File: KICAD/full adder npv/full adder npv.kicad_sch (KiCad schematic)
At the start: 24 parts, among them J2 Barrel_Jack, SW1 SW_SPDT, SW10 SW_SPDT, SW11 SW_SPDT, SW12 SW_SPDT, SW13 SW_SPDT, SW14 SW_SPDT, SW15 SW_SPDT, SW16 SW_SPDT, SW2 SW_SPDT, SW3 SW_SPDT, SW4 SW_SPDT, SW5 SW_SPDT, SW6 SW_SPDT, SW7 SW_SPDT, SW8 SW_SPDT, SW9 SW_SPDT

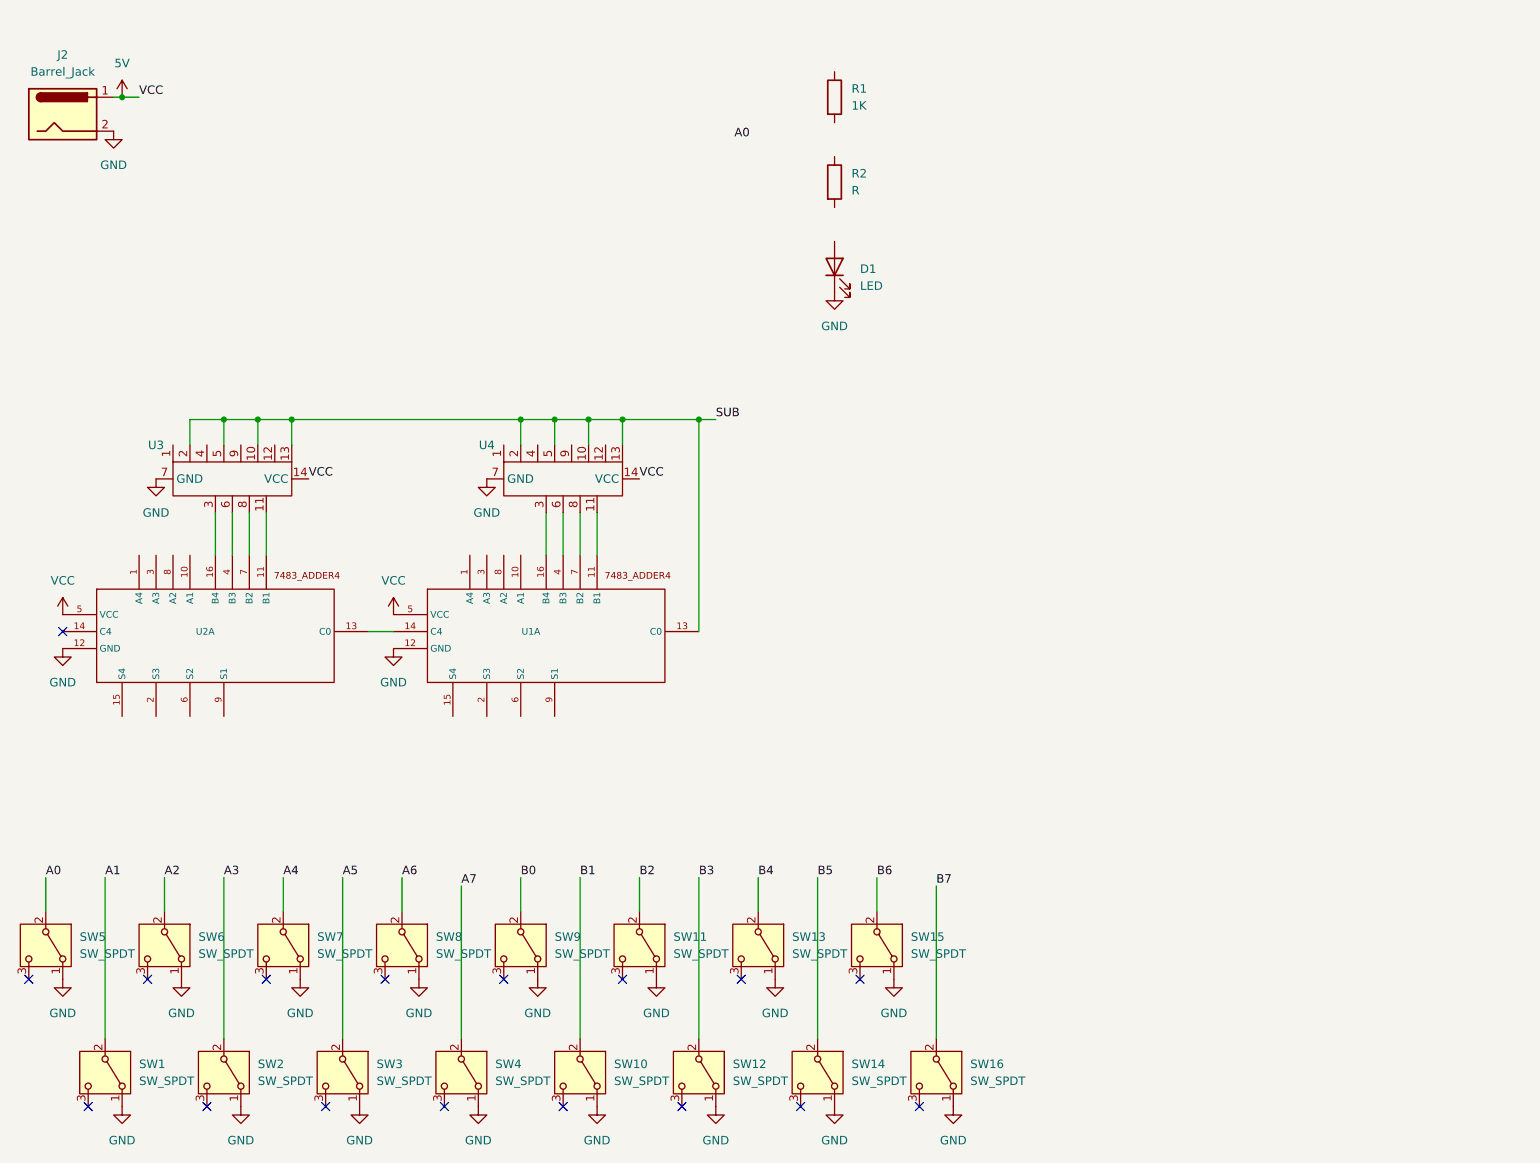
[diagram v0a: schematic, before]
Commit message: Update full adder npv.kicad_sch
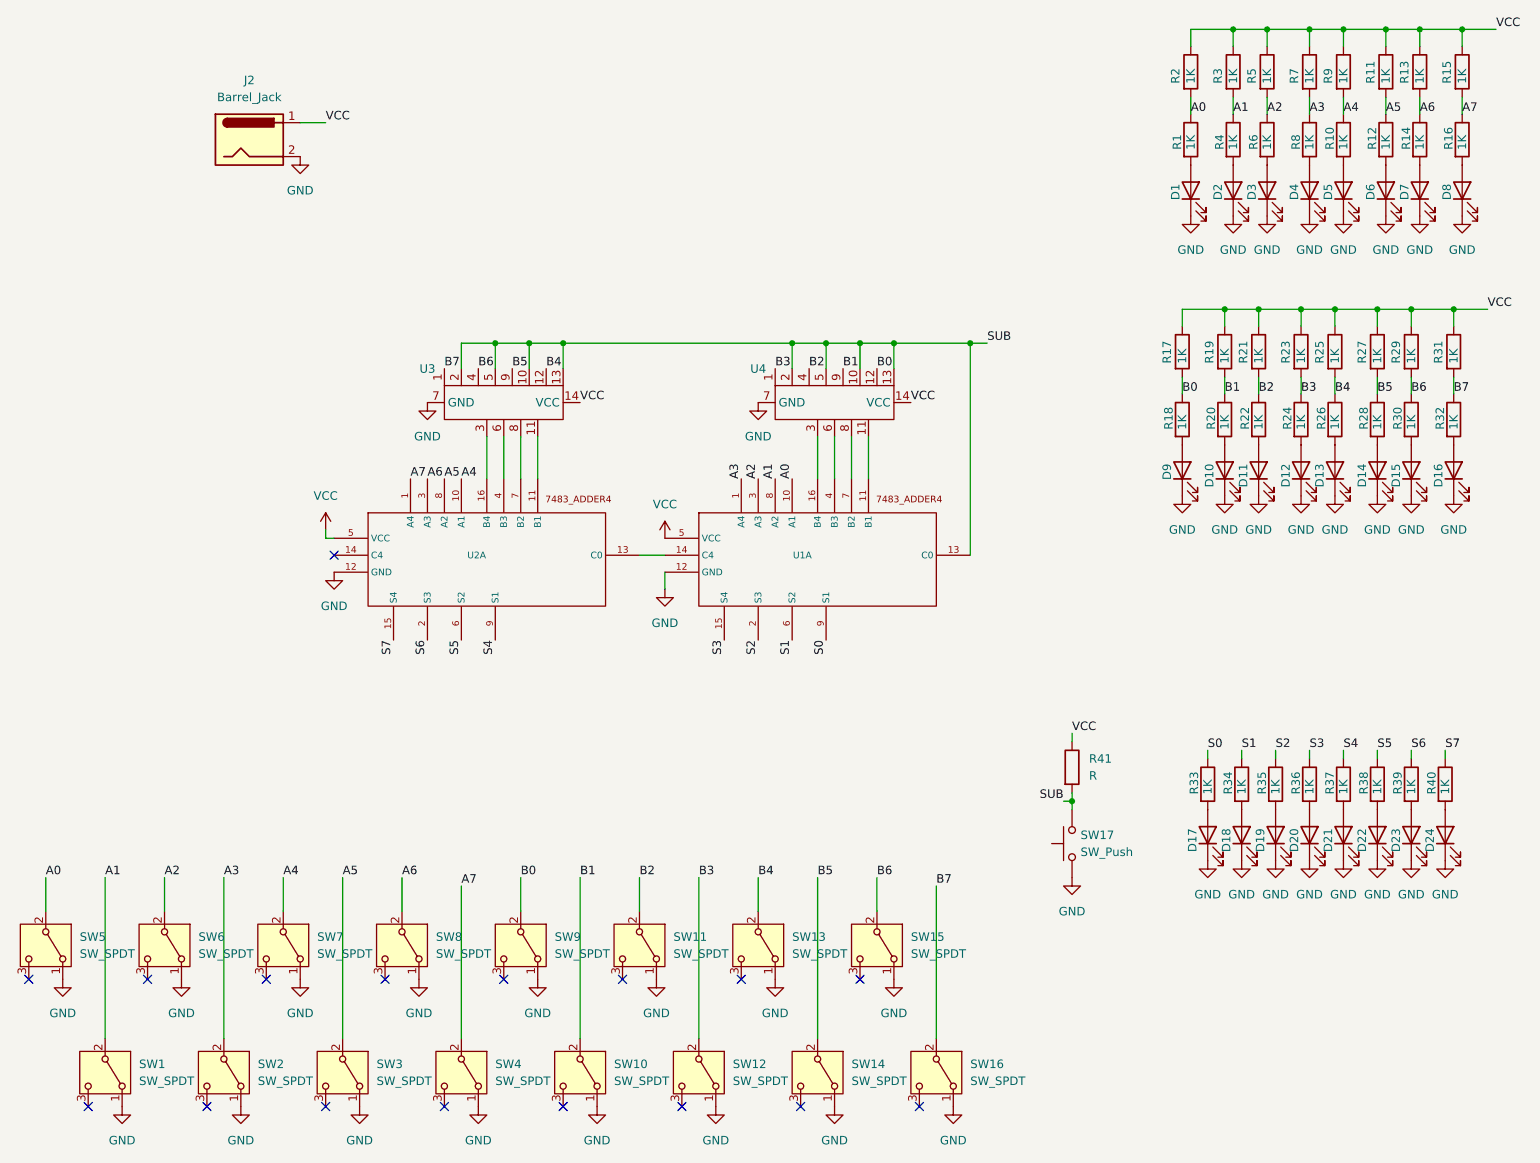
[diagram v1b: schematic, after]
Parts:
- added D10, D11, D12, D13, D14, D15, D16, D17, D18, D19, D2, D20, D21, D22, D23, D24, D3, D4, D5, D6, D7, D8, D9: LED, symbol Device:LED
- added R10, R11, R12, R13, R14, R15, R16, R17, R18, R19, R20, R21, R22, R23, R24, R25, R26, R27, R28, R29, R3, R30, R31, R32, R33, R34, R35, R36, R37, R38, R39, R4, R40, R5, R6, R7, R8, R9: 1K, symbol Device:R
- added R41: R, symbol Device:R
- added SW17: SW_Push, symbol Switch:SW_Push
- R2: value R -> 1K
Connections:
- net 5V is gone; now on net VCC: J2.1, U1.5 (VCC), U2.5 (VCC), U3.14 (VCC), U4.14 (VCC)
- net A0: now also R1.1, R2.2, U1.10 (A1)
- net A1: now also U1.8 (A2), R3.2, R4.1
- net A2: now also U1.3 (A3), R5.2, R6.1
- net A3: now also U1.1 (A4), R7.2, R8.1
- net A4: now also U2.10 (A1), R10.1, R9.2
- net A5: now also U2.8 (A2), R11.2, R12.1
- net A6: now also U2.3 (A3), R13.2, R14.1
- net A7: now also U2.1 (A4), R15.2, R16.1
- net B0: now also U4.12, R17.2, R18.1
- net B1: now also U4.9, R19.2, R20.1
- net B2: now also U4.4, R21.2, R22.1
- net B3: now also U4.1, R23.2, R24.1
- net B4: now also U3.12, R25.2, R26.1
- net B5: now also U3.9, R27.2, R28.1
- net B6: now also U3.4, R29.2, R30.1
- net B7: now also U3.1, R31.2, R32.1
- net GND: now also D10.1 (K), D11.1 (K), D12.1 (K), D13.1 (K), D14.1 (K), D15.1 (K), D16.1 (K), D17.1 (K), D18.1 (K), D19.1 (K), D2.1 (K), D20.1 (K), D21.1 (K), D22.1 (K), D23.1 (K), D24.1 (K), D3.1 (K), D4.1 (K), D5.1 (K), D6.1 (K), D7.1 (K), D8.1 (K), D9.1 (K), SW17.1
- net SUB: now also R41.2, SW17.2
- net VCC: now reaches R2.1
- net VCC: now also R11.1, R13.1, R15.1, R17.1, R19.1, R21.1, R23.1, R25.1, R27.1, R29.1, R3.1, R31.1, R41.1, R5.1, R7.1, R9.1
- net at D1.2 (A): now also R1.2
- net S7: now reaches U2.15 (S4)
- net S7: now also R40.1
- net S6: now reaches U2.2 (S3)
- net S6: now also R39.1
- net S5: now reaches U2.6 (S2)
- net S5: now also R38.1
- net S4: now reaches U2.9 (S1)
- net S4: now also R37.1
- net S3: now reaches U1.15 (S4)
- net S3: now also R36.1
- net S2: now reaches U1.2 (S3)
- net S2: now also R35.1
- net S1: now reaches U1.6 (S2)
- net S1: now also R34.1
- net S0: now reaches U1.9 (S1)
- net S0: now also R33.1
- new net: D7.2 (A), R14.2
- new net: D8.2 (A), R16.2
- new net: D16.2 (A), R32.2
- new net: D21.2 (A), R37.2
- new net: D17.2 (A), R33.2
- new net: D9.2 (A), R18.2
- new net: D19.2 (A), R35.2
- new net: D10.2 (A), R20.2
- new net: D13.2 (A), R26.2
- new net: D20.2 (A), R36.2
- new net: D18.2 (A), R34.2
- new net: D14.2 (A), R28.2
- new net: D6.2 (A), R12.2
- new net: D22.2 (A), R38.2
- new net: D15.2 (A), R30.2
- new net: D4.2 (A), R8.2
- new net: D5.2 (A), R10.2
- new net: D23.2 (A), R39.2
- new net: D11.2 (A), R22.2
- new net: D3.2 (A), R6.2
- new net: D24.2 (A), R40.2
- new net: D12.2 (A), R24.2
- new net: D2.2 (A), R4.2
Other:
- moved on the sheet: D1, J2, R1, U1A, U2A, U3, U4

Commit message: abc
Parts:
- D1, D10, D11, D12, D13, D14, D15, D16, D17, D18, D19, D2, D20, D21, D22, D23, D24, D3, D4, D5, D6, D7, D8, D9: footprint (none) -> LED_THT:LED_D3.0mm
- R1, R10, R11, R12, R13, R14, R15, R16, R17, R18, R19, R2, R20, R21, R22, R23, R24, R25, R26, R27, R28, R29, R3, R30, R31, R32, R33, R34, R35, R36, R37, R38, R39, R4, R40, R41, R5, R6, R7, R8, R9: footprint (none) -> Resistor_THT:R_Axial_DIN0204_L3.6mm_D1.6mm_P5.08mm_Horizontal
- U1, U2, U3, U4: footprint (none) -> Package_DIP:DIP-16_W7.62mm

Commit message: abc
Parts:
- J2: footprint (none) -> Connector_BarrelJack:BarrelJack_Horizontal
- SW1, SW10, SW11, SW12, SW13, SW14, SW15, SW16, SW17, SW2, SW3, SW4, SW5, SW6, SW7, SW8, SW9: footprint (none) -> Library:switch1
- U3, U4: footprint Package_DIP:DIP-16_W7.62mm -> Package_DIP:DIP-14_W7.62mm
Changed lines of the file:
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@@
 			)
 		)
-		(property "Footprint" "Package_DIP:DIP-16_W7.62mm"
+		(property "Footprint" "Package_DIP:DIP-14_W7.62mm"
 			(at 97.79 78.74 0)
 			(effects
@@
 			)
 		)
-		(property "Footprint" ""
+		(property "Footprint" "Library:switch1"
 			(at 54.61 179.07 0)
 			(effects
@@
 			)
 		)
-		(property "Footprint" ""
+		(property "Footprint" "Library:switch1"
 			(at 125.73 179.07 0)
 			(effects
@@
 			)
 		)
-		(property "Footprint" ""
+		(property "Footprint" "Library:switch1"
 			(at 63.5 160.02 0)
 			(effects
@@
 			)
 		)
-		(property "Footprint" ""
+		(property "Footprint" "Library:switch1"
 			(at 36.83 179.07 0)
 			(effects
@@
 			)
 		)
-		(property "Footprint" "Package_DIP:DIP-16_W7.62mm"
+		(property "Footprint" "Package_DIP:DIP-14_W7.62mm"
 			(at 147.32 78.74 0)
 			(effects
@@
 			)
 		)
-		(property "Footprint" ""
+		(property "Footprint" "Library:switch1"
 			(at 45.72 160.02 0)
 			(effects
@@
 			)
 		)
-		(property "Footprint" ""
+		(property "Footprint" "Library:switch1"
 			(at 72.39 179.07 0)
 			(effects
@@
 			)
 		)
-		(property "Footprint" ""
+		(property "Footprint" "Library:switch1"
 			(at 116.84 160.02 0)
 			(effects
@@
 			)
 		)
-		(property "Footprint" ""
+		(property "Footprint" "Library:switch1"
 			(at 90.17 179.07 0)
 			(effects
@@
 			)
 		)
-		(property "Footprint" ""
+		(property "Footprint" "Library:switch1"
 			(at 152.4 160.02 0)
 			(effects
@@
 			)
 		)
-		(property "Footprint" ""
+		(property "Footprint" "Library:switch1"
 			(at 81.28 160.02 0)
 			(effects
@@
 			)
 		)
-		(property "Footprint" ""
+		(property "Footprint" "Connector_BarrelJack:BarrelJack_Horizontal"
 			(at 59.69 40.386 0)
 			(effects
@@
 			)
 		)
-		(property "Footprint" ""
+		(property "Footprint" "Library:switch1"
 			(at 107.95 179.07 0)
 			(effects
@@
 			)
 		)
-		(property "Footprint" ""
+		(property "Footprint" "Library:switch1"
 			(at 176.53 144.78 0)
 			(effects
@@
 			)
 		)
-		(property "Footprint" ""
+		(property "Footprint" "Library:switch1"
 			(at 27.94 160.02 0)
 			(effects
@@
 			)
 		)
-		(property "Footprint" ""
+		(property "Footprint" "Library:switch1"
 			(at 99.06 160.02 0)
 			(effects
@@
 			)
 		)
-		(property "Footprint" ""
+		(property "Footprint" "Library:switch1"
 			(at 161.29 179.07 0)
 			(effects
@@
 			)
 		)
-		(property "Footprint" ""
+		(property "Footprint" "Library:switch1"
 			(at 134.62 160.02 0)
 			(effects
@@
 			)
 		)
-		(property "Footprint" ""
+		(property "Footprint" "Library:switch1"
 			(at 143.51 179.07 0)
 			(effects
